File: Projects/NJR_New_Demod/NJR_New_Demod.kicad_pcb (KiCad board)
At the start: 2 copper layers, 86.4 x 50.8 mm, 27 parts, among them J1 SMA-J-P-H-ST-EM1, U1 SFECF10M7EA00-R0, U2 NJM2549, U3 NJM2741

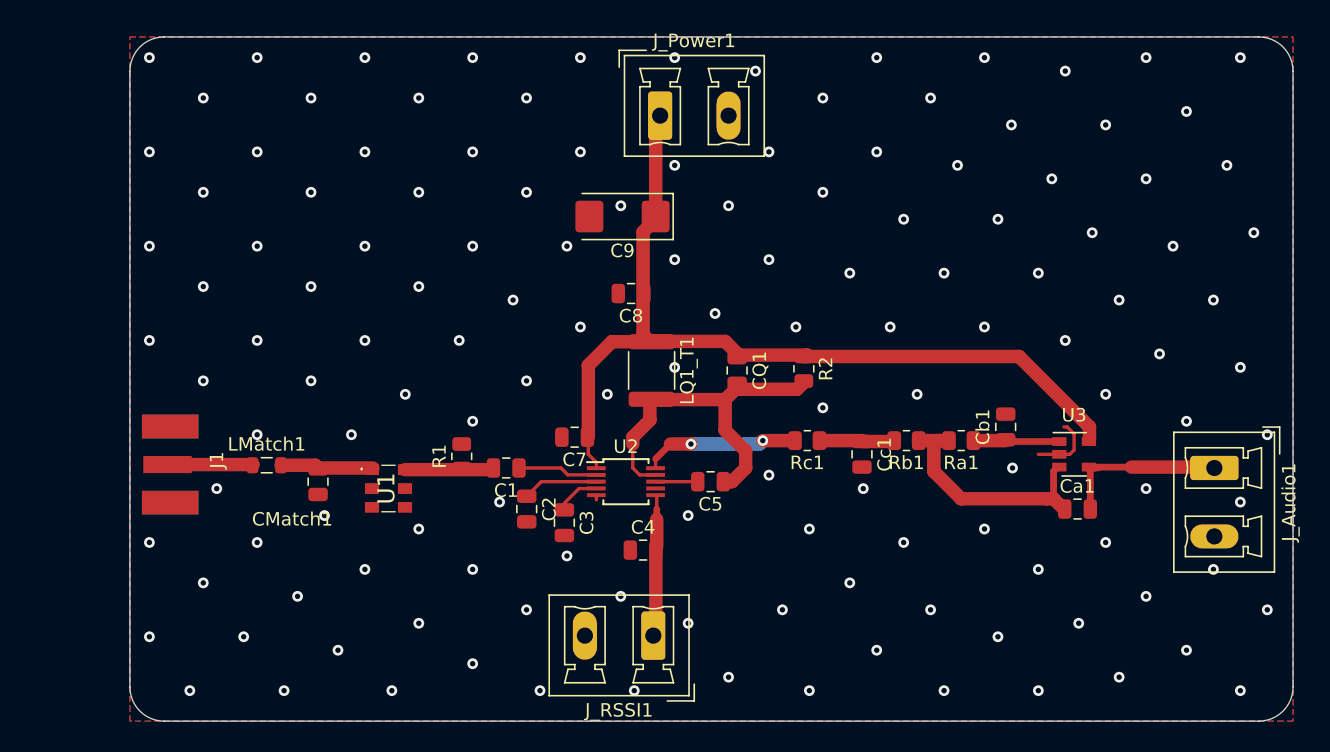
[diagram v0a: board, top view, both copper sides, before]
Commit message: Added a VVA
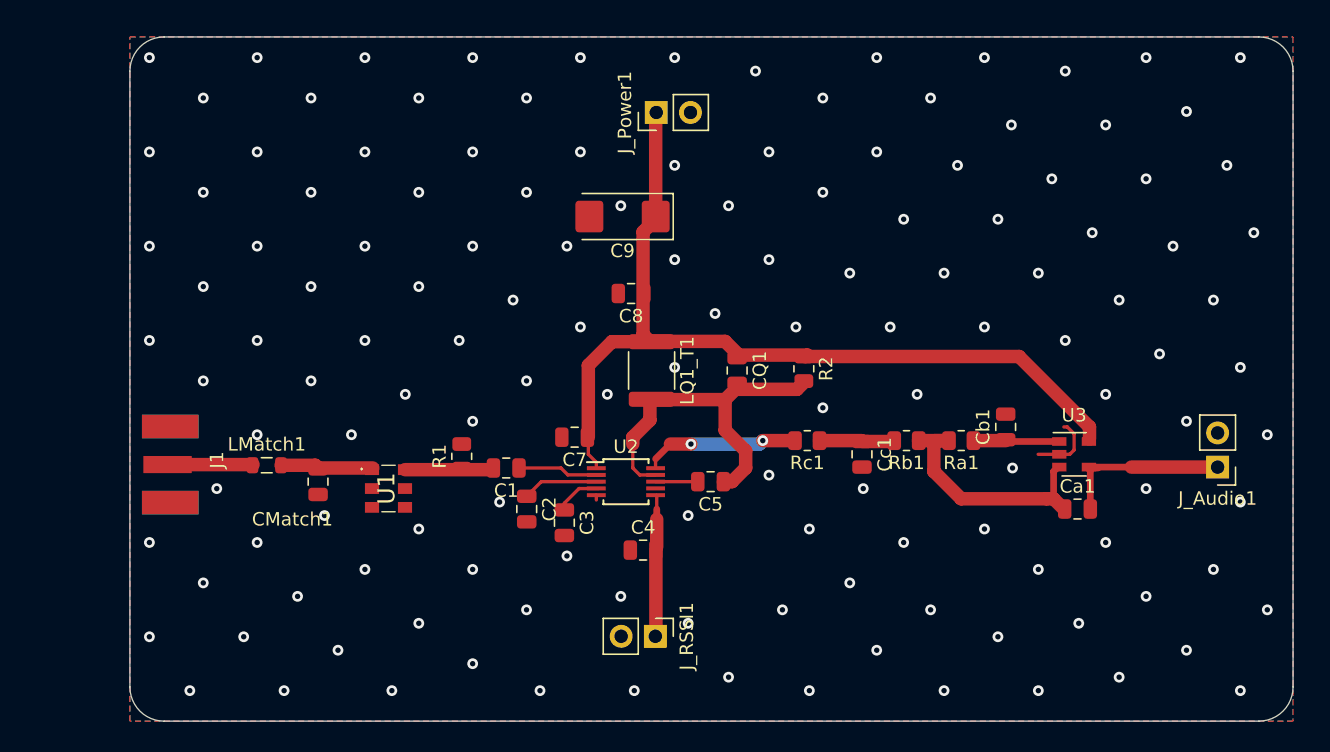
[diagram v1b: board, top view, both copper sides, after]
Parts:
- J_Audio1, J_Power1, J_RSSI1: footprint Connector_Phoenix_MC_HighVoltage:PhoenixContact_MCV_1,5_2-G-5.08_1x02_P5.08mm_Vertical -> Connector_PinHeader_2.54mm:PinHeader_1x02_P2.54mm_Vertical
- moved J_Power1 0.37 mm to (115.3, 64.0), turned to 90 degrees
- moved J_Audio1 0.25 mm to (157.0, 90.4), turned to 180 degrees
- moved J_RSSI1 0.16 mm to (115.2, 102.9), turned to 270 degrees

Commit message: Power Detector and power splitter boards designed
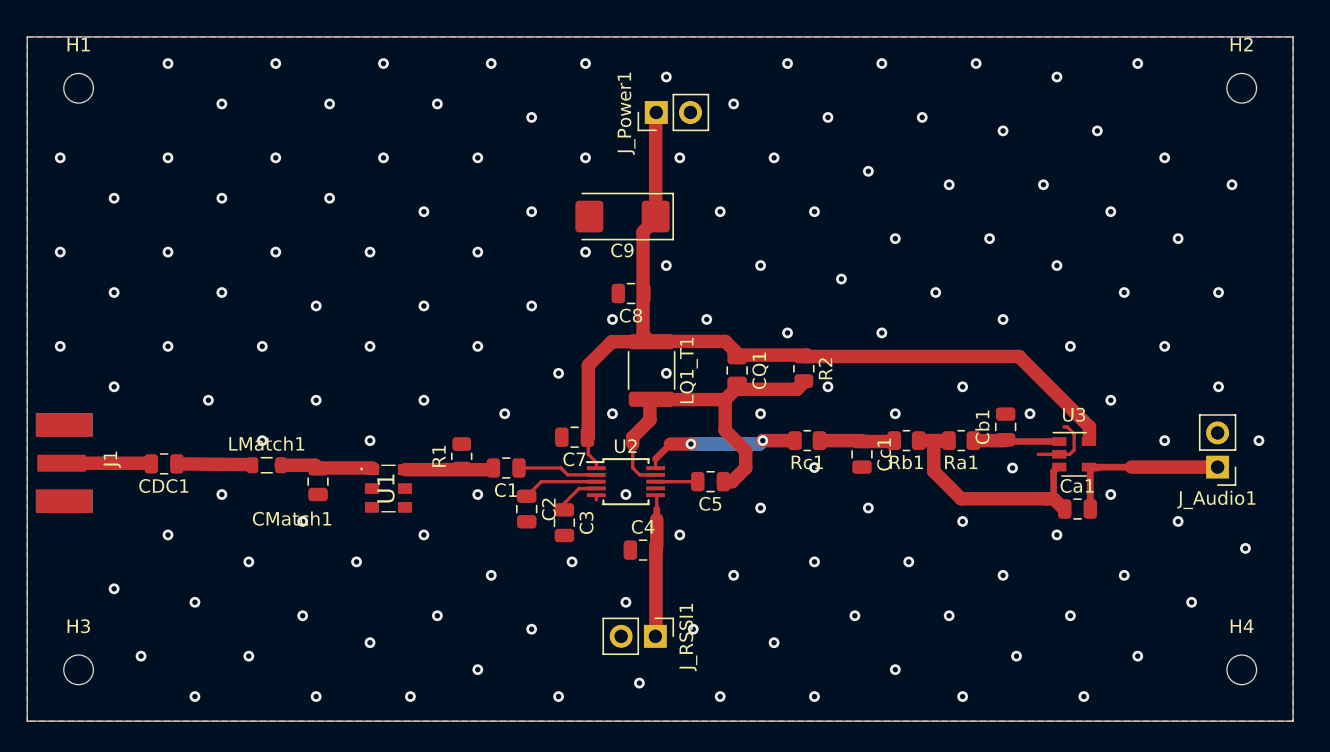
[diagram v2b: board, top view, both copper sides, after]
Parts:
- added CDC1: .1u, Capacitor_SMD:C_0805_2012Metric, F.Cu at (78.7, 90.1)
- added H1: MountingHole, MountingHole:MountingHole_2.2mm_M2, F.Cu at (72.4, 62.2)
- added H2: MountingHole, MountingHole:MountingHole_2.2mm_M2, F.Cu at (158.8, 62.2)
- added H3: MountingHole, MountingHole:MountingHole_2.2mm_M2, F.Cu at (72.4, 105.4)
- added H4: MountingHole, MountingHole:MountingHole_2.2mm_M2, F.Cu at (158.8, 105.4)
- moved J1 7.87 mm to (71.1, 90.1)
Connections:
- J1 pad 1: Net-(J1-Pad1) -> Net-(CDC1-Pad2)
- LMatch1 pad 1: Net-(J1-Pad1) -> Net-(CDC1-Pad1)
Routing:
- net Net-(J1-Pad1): track 6.60 -> 0.00 mm
- net Net-(CDC1-Pad2): track 0.00 -> 6.25 mm
- net Net-(CDC1-Pad1): track 0.00 -> 5.40 mm
- net GND: vias 138 -> 146
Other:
- board size 86.4 x 50.8 mm -> 94 x 50.8 mm
